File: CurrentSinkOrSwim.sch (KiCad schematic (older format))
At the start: 3 parts, among them P101 CONN_01X02, P102 CONN_01X03, P103 CONN_01X02

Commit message: Preliminary association of components and placement into layout.
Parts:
- P101, P103: footprint (none) -> Pin_Headers:Pin_Header_Angled_1x02
- P102: footprint (none) -> Pin_Headers:Pin_Header_Angled_1x03
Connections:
- wire segments 22 -> 17
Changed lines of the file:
@@
 F 0 "P103" H 8300 1450 50  0000 C CNN
 F 1 "CONN_01X02" V 8400 1300 50  0000 C CNN
-F 2 "" H 8300 1300 60  0000 C CNN
+F 2 "Pin_Headers:Pin_Header_Angled_1x02" H 8300 1300 60  0001 C CNN
 F 3 "" H 8300 1300 60  0000 C CNN
 	1    8300 1300
@@
 F 0 "P102" H 6850 800 50  0000 C CNN
 F 1 "CONN_01X03" V 6950 600 50  0000 C CNN
-F 2 "" H 6850 600 60  0000 C CNN
+F 2 "Pin_Headers:Pin_Header_Angled_1x03" H 6850 600 60  0001 C CNN
 F 3 "" H 6850 600 60  0000 C CNN
 	1    6850 600
@@
 F 0 "P101" H 3000 1000 50  0000 C CNN
 F 1 "CONN_01X02" V 3100 850 50  0000 C CNN
-F 2 "" H 3000 850 60  0000 C CNN
+F 2 "Pin_Headers:Pin_Header_Angled_1x02" H 3000 850 60  0001 C CNN
 F 3 "" H 3000 850 60  0000 C CNN
 	1    3000 850
@@
 $EndComp
 $Comp
-L GND #PWR101
+L GND #PWR01
 U 1 1 54D85A15
 P 3350 1450
-F 0 "#PWR101" H 3350 1200 60  0001 C CNN
+F 0 "#PWR01" H 3350 1200 60  0001 C CNN
 F 1 "GND" H 3350 1300 60  0000 C CNN
 F 2 "" H 3350 1450 60  0000 C CNN
@@
 	8100 1350 7900 1350
 Wire Wire Line
-	7900 1350 7900 4350
+	7900 1350 7900 6250
 Wire Wire Line
-	7900 4350 7900 6250
-Wire Wire Line
-	7500 1250 7500 1250
-Wire Wire Line
-	7500 1250 7500 1250
-Wire Wire Line
-	7500 1250 8100 1250
-Wire Wire Line
-	7500 1250 6950 1250
+	6950 1250 8100 1250
 Wire Wire Line
 	6950 1250 6950 800
@@
 	3350 900  3350 1450
 Wire Wire Line
-	7500 1250 7500 3550
-Wire Wire Line
-	7500 3550 7500 5500
+	7500 1250 7500 5500
 Connection ~ 7500 1250
 Wire Wire Line
@@
 	4550 4400 4800 4400
 $Comp
-L GND #PWR102
+L GND #PWR02
 U 1 1 54DB4AD2
 P 7900 6250
-F 0 "#PWR102" H 7900 6000 60  0001 C CNN
+F 0 "#PWR02" H 7900 6000 60  0001 C CNN
 F 1 "GND" H 7900 6100 60  0000 C CNN
 F 2 "" H 7900 6250 60  0000 C CNN

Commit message: Added new potentiometer footprints to layout
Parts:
- P101, P103: footprint Pin_Headers:Pin_Header_Angled_1x02 -> Current:Terminal_Block_200_mil; MPN (none) -> OSTTC022162
- P102: footprint Pin_Headers:Pin_Header_Angled_1x03 -> Pin_Headers:Pin_Header_Straight_1x03
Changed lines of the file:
@@
 F 0 "P103" H 8300 1450 50  0000 C CNN
 F 1 "CONN_01X02" V 8400 1300 50  0000 C CNN
-F 2 "Pin_Headers:Pin_Header_Angled_1x02" H 8300 1300 60  0001 C CNN
+F 2 "Current:Terminal_Block_200_mil" H 8300 1300 60  0001 C CNN
 F 3 "" H 8300 1300 60  0000 C CNN
+F 4 "OSTTC022162" H 8300 1300 60  0001 C CNN "MPN"
 	1    8300 1300
 	1    0    0    -1
@@
 F 0 "P102" H 6850 800 50  0000 C CNN
 F 1 "CONN_01X03" V 6950 600 50  0000 C CNN
-F 2 "Pin_Headers:Pin_Header_Angled_1x03" H 6850 600 60  0001 C CNN
+F 2 "Pin_Headers:Pin_Header_Straight_1x03" H 6850 600 60  0001 C CNN
 F 3 "" H 6850 600 60  0000 C CNN
 	1    6850 600
@@
 F 0 "P101" H 3000 1000 50  0000 C CNN
 F 1 "CONN_01X02" V 3100 850 50  0000 C CNN
-F 2 "Pin_Headers:Pin_Header_Angled_1x02" H 3000 850 60  0001 C CNN
+F 2 "Current:Terminal_Block_200_mil" H 3000 850 60  0001 C CNN
 F 3 "" H 3000 850 60  0000 C CNN
+F 4 "OSTTC022162" H 3000 850 60  0001 C CNN "MPN"
 	1    3000 850
 	-1   0    0    -1

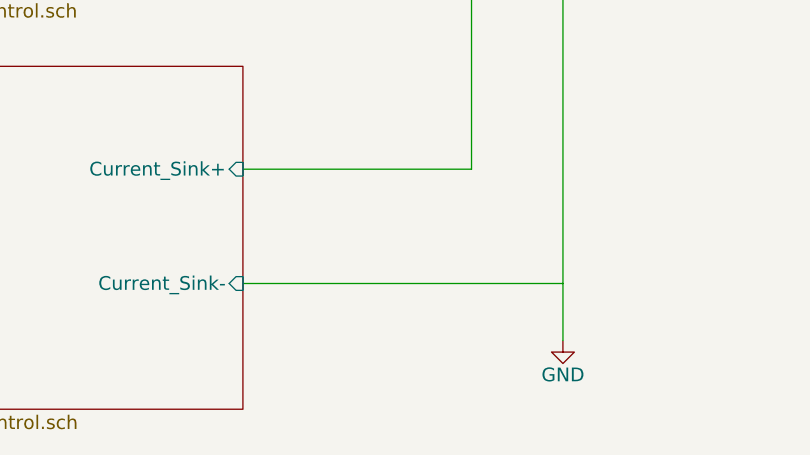
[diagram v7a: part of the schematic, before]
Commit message: Moved pots/terms and routed traces to all components
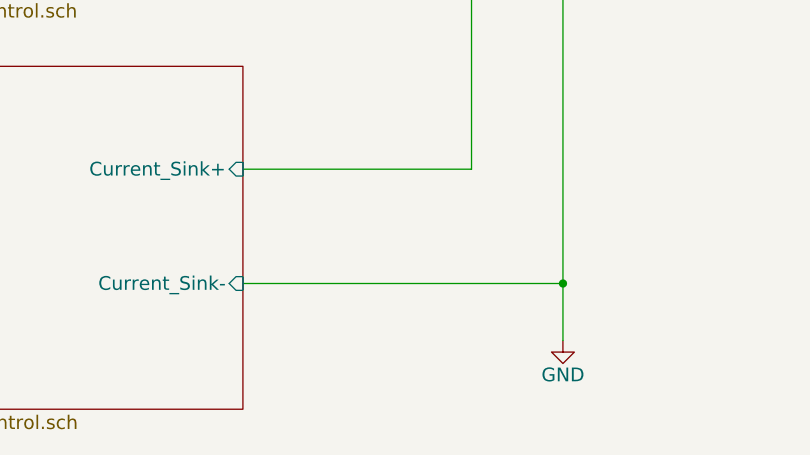
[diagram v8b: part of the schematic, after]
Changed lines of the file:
@@
 	7500 5500 6500 5500
 Connection ~ 7500 3550
-Wire Wire Line
-	7900 6000 6500 6000
 Connection ~ 7900 4350
 Wire Wire Line
@@
 Wire Wire Line
 	3200 800  6750 800
+Wire Wire Line
+	6500 6000 7900 6000
+Connection ~ 7900 6000
 $EndSCHEMATC
